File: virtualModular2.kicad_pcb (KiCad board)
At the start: 2 copper layers, 100 x 164 mm, 125 parts, among them CON1 BARREL_JACK, P1 POWER, P18 3VI2C, P19 PIGPIO, P2 FTDI, P3 5V SPI, P4 I2C, Q1 BSS138, Q2 BSS138, SW10 SW_PUSH, SW11 SW_PUSH, SW12 SW_PUSH, SW13 SW_PUSH, SW14 SW_PUSH, SW2 ROTARY_ENCODER_SWITCH, SW3 SW_PUSH, SW4 SW_PUSH, SW5 SW_PUSH, SW6 SW_PUSH, SW7 SW_PUSH, SW8 SW_PUSH, SW9 SW_PUSH, U1 NCP1117ST50T3G

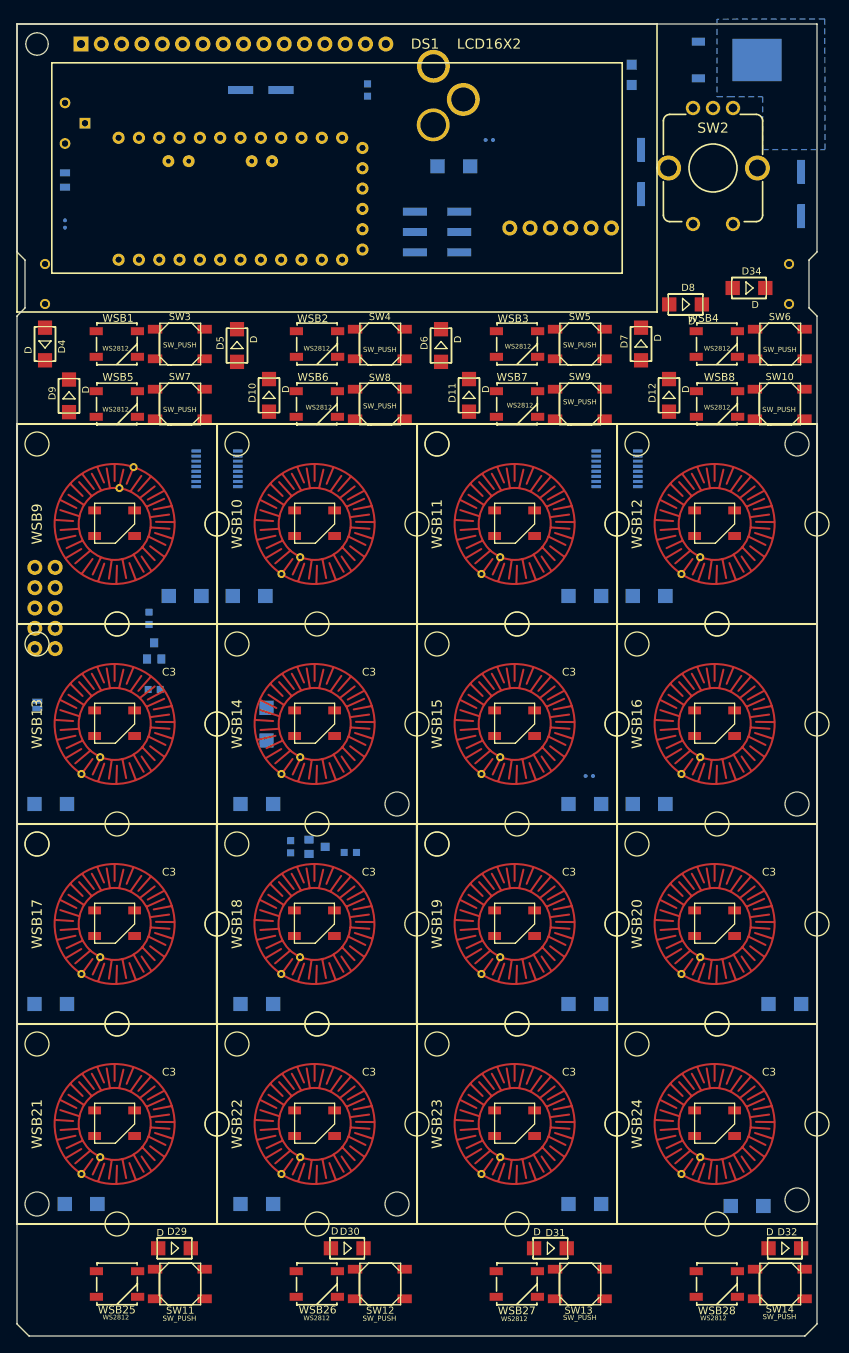
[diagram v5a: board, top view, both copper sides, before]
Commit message: add midi io to the board
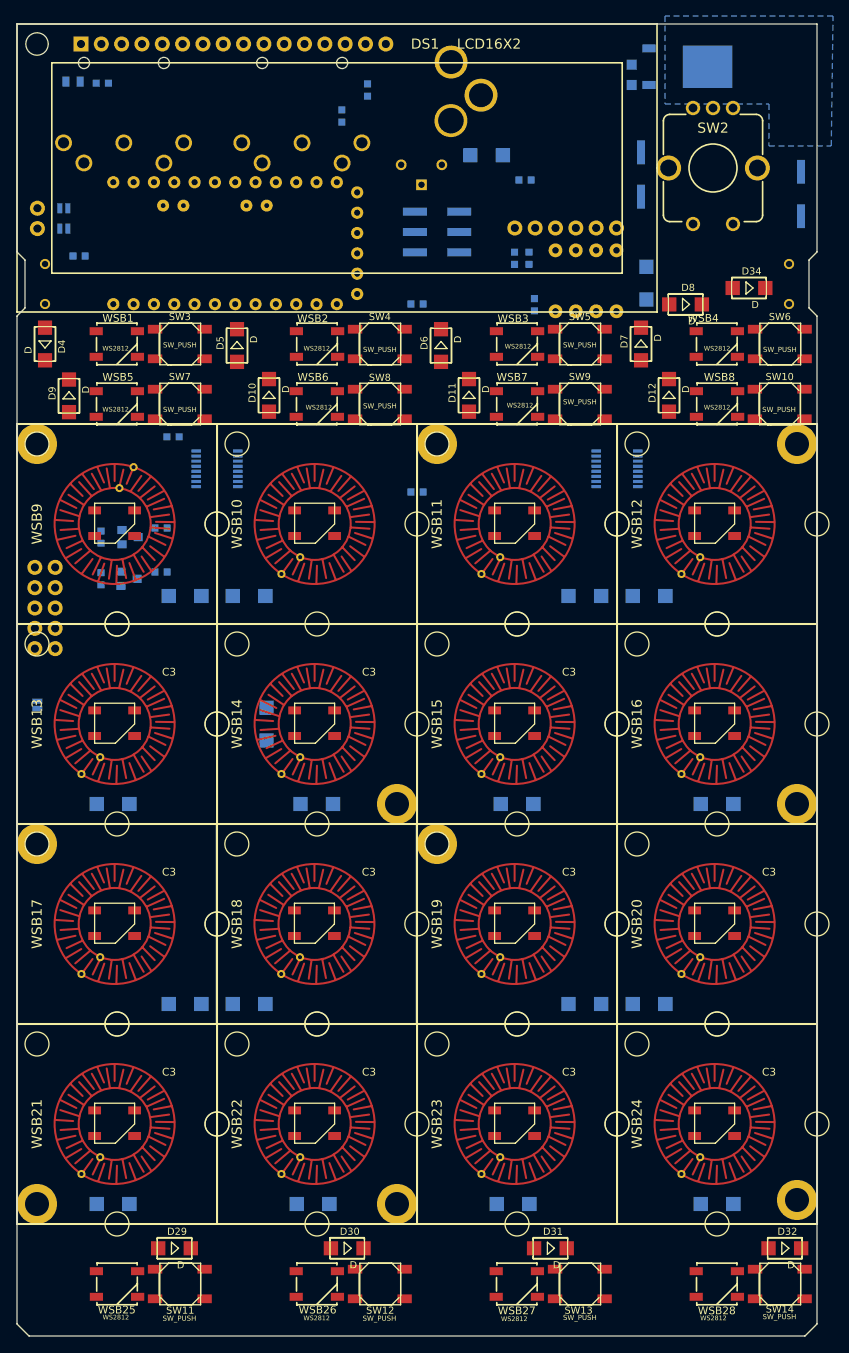
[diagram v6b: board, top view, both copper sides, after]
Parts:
- added D3: D, SeeedOPL-Diode:DO-214AC, B.Cu at (78.7, 32.4)
- added JP1: D11->MIDITX, SparkFun-Passives:PAD-JUMPER-2-NC_BY_TRACE_YES_SILK, B.Cu at (5.85, 25.6)
- added JP3: D10->MIDIRX, SparkFun-Passives:PAD-JUMPER-2-NC_BY_TRACE_YES_SILK, B.Cu at (5.85, 23.0)
- added P5: MIDIRXTX, SparkFun-Connectors:1X02, B.Cu at (2.55, 23.0)
- added P6: DIN_5, SparkFun-Connectors:DIN_5_FEMALE, B.Cu at (35.2, 11.2)
- added R2: R, SeeedOPL-Resistor:R0603, B.Cu at (19.5, 51.6)
- added R3: 220, SeeedOPL-Resistor:R0603, B.Cu at (50.0, 35.0)
- added R4: 4.7K, SeeedOPL-Resistor:R0603, B.Cu at (64.7, 35.1)
- added R5: 4.7K, SeeedOPL-Resistor:R0603, B.Cu at (64.0, 29.3)
- added R6: 4.7K, SeeedOPL-Resistor:R0603, B.Cu at (62.2, 29.3)
- added R7: 220, SeeedOPL-Resistor:R0603, B.Cu at (40.6, 11.5)
- added R8: 220, SeeedOPL-Resistor:R0603, B.Cu at (7.76, 29.0)
- added U2: 6N138, SparkFun-DigitalIC:DIP08, B.Cu at (71.1, 32.1)
- C1: footprint SeeedOPL-Capacitor:C0402 -> SeeedOPL-Capacitor:C0603
- C_LEDS1: value 1uF-10V -> 1uF-25V; footprint SeeedOPL-Capacitor:C0402_electrolitic -> SeeedOPL-Capacitor:C0603
- D1, D10, D11, D12, D13, D14, D15, D16, D17, D18, D19, D20, D21, D22, D23, D24, D25, D26, D27, D28, D29, D30, D31, D32, D33, D34, D4, D5, D6, D7, D8, D9: footprint lib_fp:DO-214AC -> SeeedOPL-Diode:DO-214AC
- P4: value I2C -> DIN_5; footprint Pin_Headers:Pin_Header_Straight_2x01_Pitch2.54mm_SMD -> SparkFun-Connectors:DIN_5_FEMALE
- R1: footprint SeeedOPL-Resistor:R0402 -> SeeedOPL-Resistor:R0603
- moved RV1 42.8 mm to (50.6, 20.1), turned to 0 degrees
- moved R11 42.3 mm to (18.0, 68.5)
- moved C_LEDS1 41.5 mm to (50.0, 58.5)
- moved R12 41.0 mm to (10.5, 69.3)
- moved Q1 40.9 mm to (14.0, 69.3)
- moved R14 20.2 mm to (10.5, 64.1), turned to 0 degrees
- moved R1 18.2 mm to (10.7, 7.40), turned to 90 degrees
- moved P4 17.8 mm to (12.9, 11.2)
- moved D24 17.0 mm to (79.0, 122.5)
- moved D21 16.8 mm to (21.0, 122.5)
- moved Q2 14.5 mm to (14.1, 64.1), turned to 90 degrees
- moved D2 12.3 mm to (7.00, 7.20), turned to 180 degrees
- moved R13 11.4 mm to (18.0, 63.0), turned to 270 degrees
- moved D27 8.98 mm to (62.0, 147.5)
- moved D20 8.50 mm to (87.5, 97.5)
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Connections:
- P4 pad 1: /SCL -> (no net)
- P4 pad 2: /SDA -> (no net)
- SW10 pad 1: Net-(D12-Pad-) -> Net-(D12-Pad2)
- SW11 pad 1: Net-(D29-Pad-) -> Net-(D29-Pad2)
- SW12 pad 1: Net-(D30-Pad-) -> Net-(D30-Pad2)
- SW13 pad 1: Net-(D31-Pad-) -> Net-(D31-Pad2)
- SW14 pad 1: Net-(D32-Pad-) -> Net-(D32-Pad2)
- SW2 pad E: Net-(D8-Pad-) -> Net-(D8-Pad2)
- SW3 pad 1: Net-(D4-Pad-) -> Net-(D4-Pad2)
- SW4 pad 1: Net-(D5-Pad-) -> Net-(D5-Pad2)
- SW5 pad 1: Net-(D6-Pad-) -> Net-(D6-Pad2)
- SW6 pad 1: Net-(D7-Pad-) -> Net-(D7-Pad2)
- SW7 pad 1: Net-(D9-Pad-) -> Net-(D9-Pad2)
- SW8 pad 1: Net-(D10-Pad-) -> Net-(D10-Pad2)
- SW9 pad 1: Net-(D11-Pad-) -> Net-(D11-Pad2)
- SW_left1 pad 1: Net-(D33-Pad-) -> Net-(D33-Pad2)
- SW_right1 pad 1: Net-(D34-Pad-) -> Net-(D34-Pad2)
- WSB10 pad 5: Net-(D14-Pad-) -> Net-(D14-Pad2)
- WSB11 pad 5: Net-(D15-Pad-) -> Net-(D15-Pad2)
- WSB12 pad 5: Net-(D16-Pad-) -> Net-(D16-Pad2)
- WSB13 pad 5: Net-(D17-Pad-) -> Net-(D17-Pad2)
- WSB14 pad 5: Net-(D18-Pad-) -> Net-(D18-Pad2)
- WSB15 pad 5: Net-(D19-Pad-) -> Net-(D19-Pad2)
- WSB16 pad 5: Net-(D20-Pad-) -> Net-(D20-Pad2)
- WSB17 pad 5: Net-(D21-Pad-) -> Net-(D21-Pad2)
- WSB18 pad 5: Net-(D22-Pad-) -> Net-(D22-Pad2)
- WSB19 pad 5: Net-(D23-Pad-) -> Net-(D23-Pad2)
- WSB20 pad 5: Net-(D24-Pad-) -> Net-(D24-Pad2)
- WSB21 pad 5: Net-(D25-Pad-) -> Net-(D25-Pad2)
- WSB22 pad 5: Net-(D26-Pad-) -> Net-(D26-Pad2)
- WSB23 pad 5: Net-(D27-Pad-) -> Net-(D27-Pad2)
- WSB24 pad 5: Net-(D28-Pad-) -> Net-(D28-Pad2)
- WSB9 pad 5: Net-(D13-Pad-) -> Net-(D13-Pad2)
- uP1 pad 24: /MUXA_COMMON -> /LCD5
- uP1 pad 25: /MUXB_COMMON -> /LCD4
- uP1 pad 26: /LCD5 -> /LCD3
- uP1 pad 27: /LCD4 -> /LCD2
- uP1 pad 28: /LCD3 -> /LCD1
- uP1 pad 29: /LCD2 -> Net-(JP1-Pad1)
- uP1 pad 30: /LCD1 -> Net-(JP3-Pad1)
- uP1 pad 31: /SDA -> /MUXB_COMMON
- uP1 pad 32: /SCL -> /MUXA_COMMON
